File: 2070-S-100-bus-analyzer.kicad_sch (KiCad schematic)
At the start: 3 parts, among them J1 S100

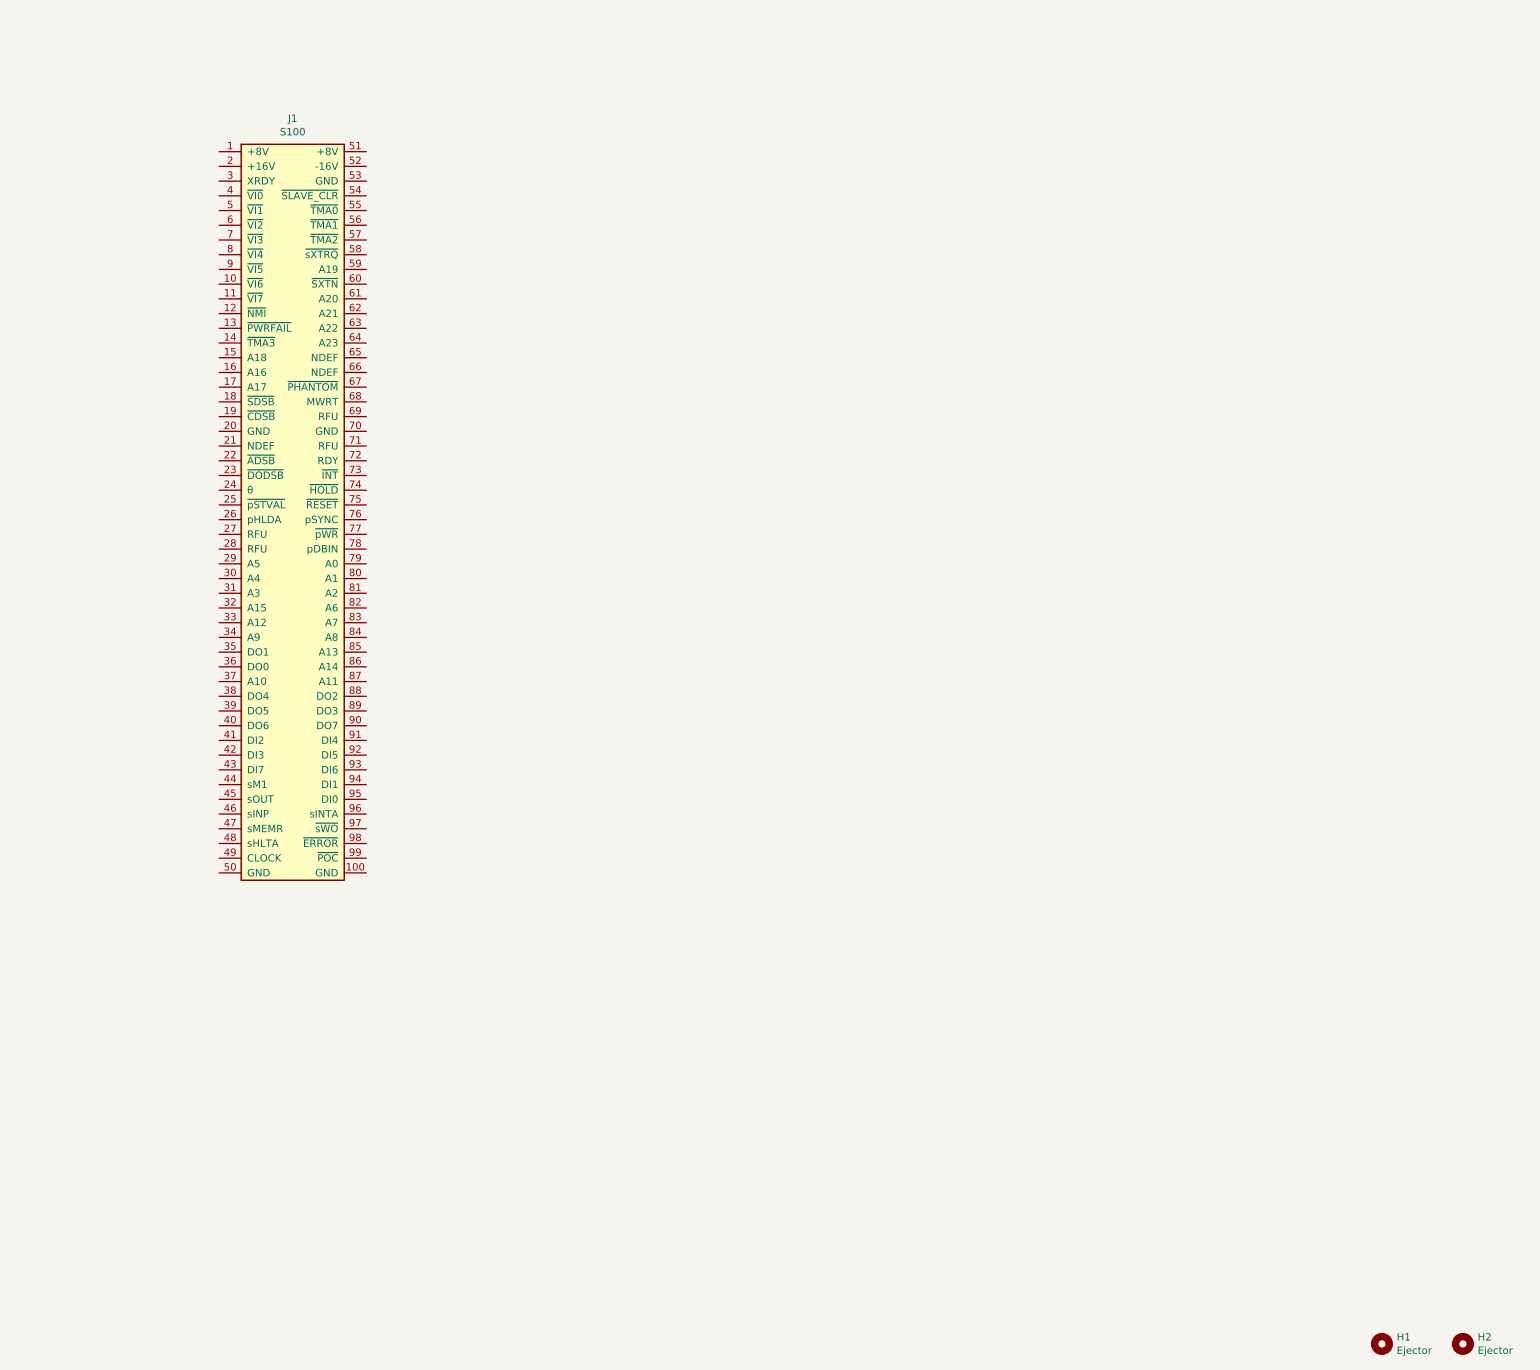
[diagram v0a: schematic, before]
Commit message: Re-start project from new KiCad9 S-100 template
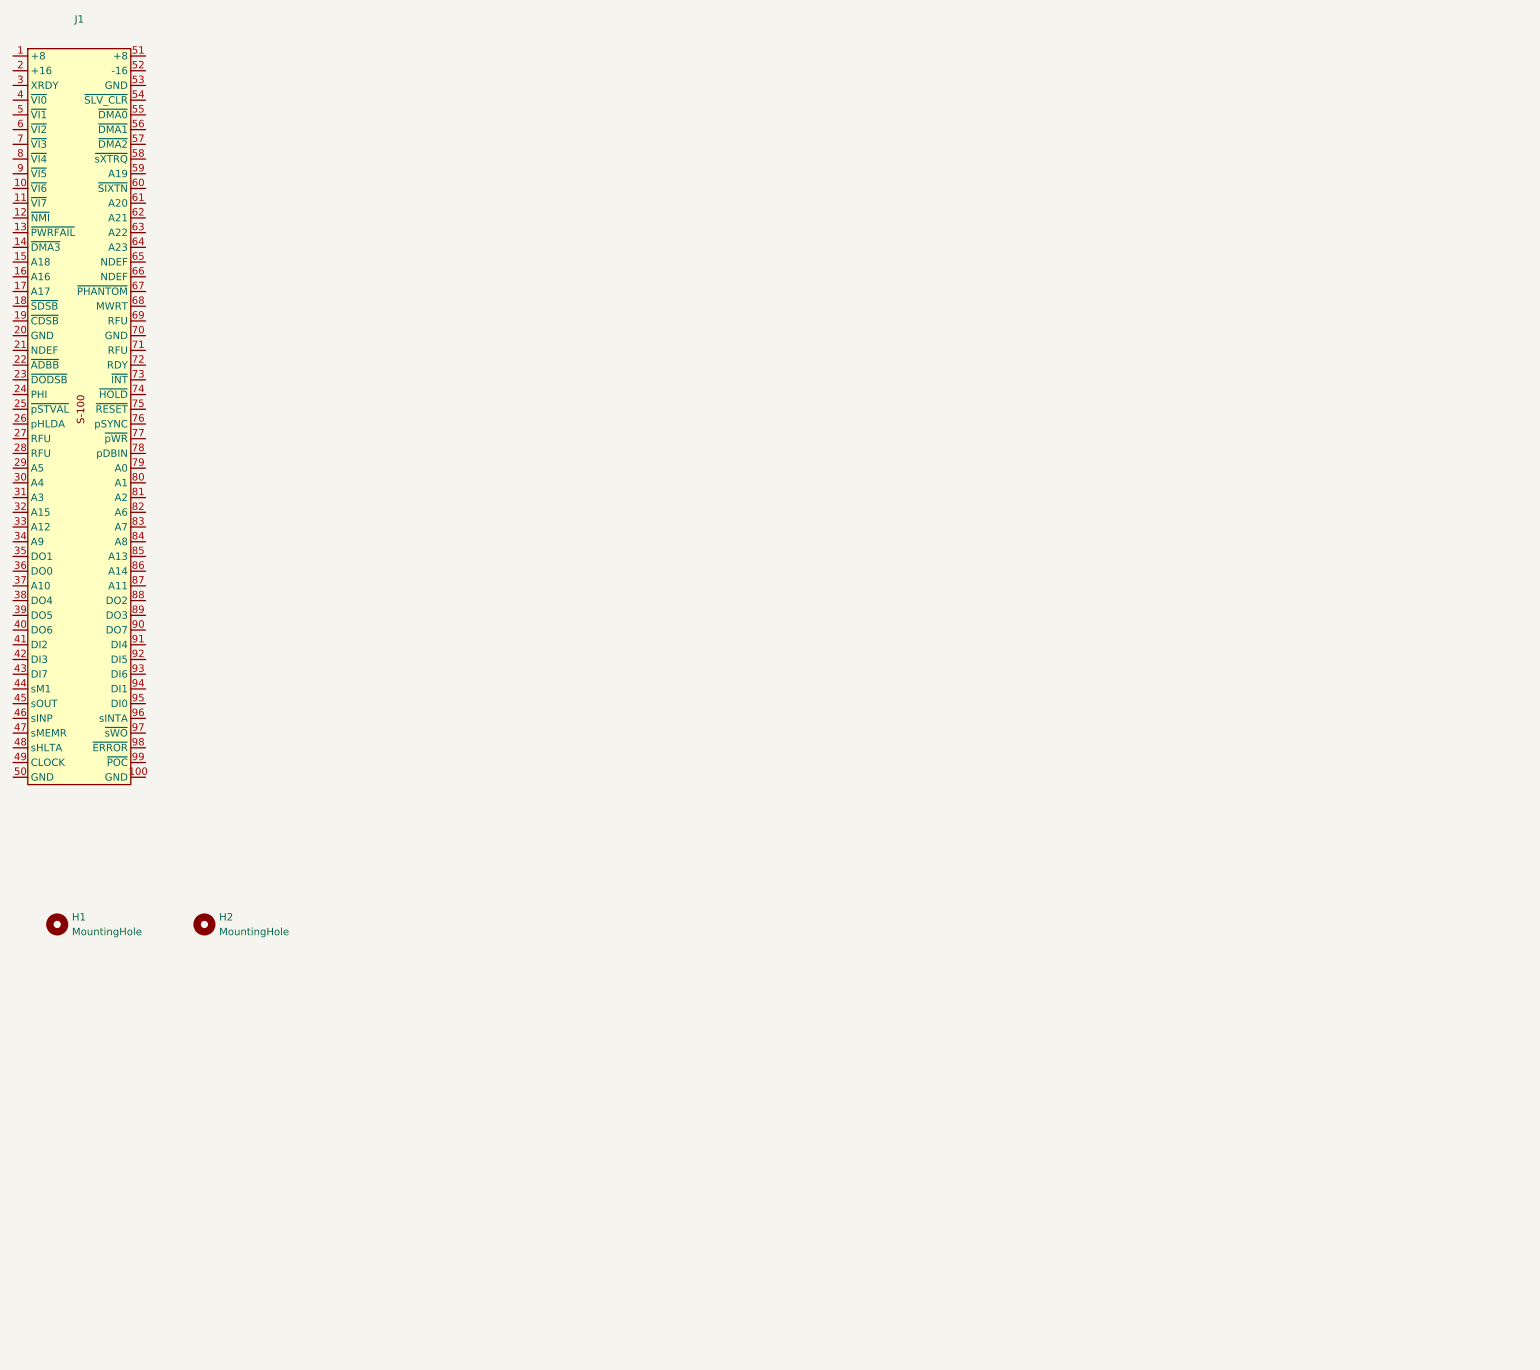
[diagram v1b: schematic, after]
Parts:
- removed J1: S100, jb-footprint:S100_MALE, symbol S-100-Template-rescue:S100-jb-symbol-S-100-Template-rescue
- added J1: ~, S100-footprints:S100-Edge-Connector, symbol S100:S100-Edge-Connector
- H1, H2: value Ejector -> MountingHole; footprint jb-footprint:MountingHole_2.7mm_M2.5 -> MountingHole:MountingHole_2.5mm; now left out of the parts list

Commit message: Checkpoint
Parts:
- added A1, A2, A3, A4, A5: RaspberryPi_Pico, Module:RaspberryPi_Pico_Common_Unspecified, symbol MCU_Module:RaspberryPi_Pico
- added D1, D2, D3: LED_Filled, LED_SMD:LED_0805_2012Metric_Pad1.15x1.40mm_HandSolder, symbol Device:LED_Filled
- added J10, J11, J2, J3, J4, J5, J6, J7, J8, J9: Conn_02x13_Odd_Even, Connector_PinHeader_2.54mm:PinHeader_2x13_P2.54mm_Vertical, symbol Connector_Generic:Conn_02x13_Odd_Even
- added U1, U10, U11, U12, U13, U14, U15, U2, U3, U4, U5, U6, U7, U8, U9: 74LVCH245APW,118, Package_SO:TSSOP-20_4.4x6.5mm_P0.65mm, symbol Logic_LevelTranslator:SN74LVC245APW
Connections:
- net at J1.10 (~{VI6}): now also J2.15 (Pin_15)
- net GND: now reaches J1.100 (GND)
- net GND: now also J1.50 (GND), J2.25 (Pin_25), J2.26 (Pin_26), J3.25 (Pin_25), J3.26 (Pin_26), J4.25 (Pin_25), J4.26 (Pin_26), J5.25 (Pin_25), J5.26 (Pin_26), J6.25 (Pin_25), J6.26 (Pin_26), J7.25 (Pin_25), J7.26 (Pin_26), J8.25 (Pin_25), J8.26 (Pin_26), J9.25 (Pin_25), J9.26 (Pin_26), U1.1 (DIR), U1.19 (~{OE})
- net at J1.11 (~{VI7}): now also J2.17 (Pin_17)
- net at J1.12 (~{NMI}): now also J2.19 (Pin_19)
- net at J1.13 (~{PWRFAIL}): now also J2.21 (Pin_21)
- net at J1.14 (~{DMA3}): now also J2.23 (Pin_23)
- net at J1.15 (A18): now also J3.1 (Pin_1)
- net at J1.16 (A16): now also J3.3 (Pin_3)
- net at J1.17 (A17): now also J3.5 (Pin_5)
- net at J1.18 (~{SDSB}): now also J3.7 (Pin_7)
- net at J1.19 (~{CDSB}): now also J3.9 (Pin_9)
- net at J1.20 (GND): now also J3.11 (Pin_11)
- net at J1.21 (NDEF): now also J3.13 (Pin_13)
- net at J1.22 (~{ADSB}): now also J3.15 (Pin_15)
- net at J1.23 (~{DODSB}): now also J3.17 (Pin_17)
- net at J1.24 (PHI): now also J3.19 (Pin_19)
- net at J1.25 (~{pSTVAL}): now also J3.21 (Pin_21)
- net at J1.26 (pHLDA): now also J3.23 (Pin_23)
- net at J1.27 (RFU): now also J4.1 (Pin_1)
- net at J1.28 (RFU): now also J4.3 (Pin_3)
- net at J1.29 (A5): now also J4.5 (Pin_5)
- net at J1.3 (XRDY): now also J2.1 (Pin_1)
- net at J1.30 (A4): now also J4.7 (Pin_7)
- net at J1.31 (A3): now also J4.9 (Pin_9)
- net at J1.32 (A15): now also J4.11 (Pin_11)
- net at J1.33 (A12): now also J4.13 (Pin_13)
- net at J1.34 (A9): now also J4.15 (Pin_15)
- net at J1.35 (DO1): now also J4.17 (Pin_17)
- net at J1.36 (DO0): now also J4.19 (Pin_19)
- net at J1.37 (A10): now also J4.21 (Pin_21)
- net at J1.38 (DO4): now also J4.23 (Pin_23)
- net at J1.39 (DO5): now also J5.1 (Pin_1)
- net at J1.4 (~{VI0}): now also J2.3 (Pin_3)
- net at J1.40 (DO6): now also J5.3 (Pin_3)
- net at J1.41 (DI2): now also J5.5 (Pin_5)
- net at J1.42 (DI3): now also J5.7 (Pin_7)
- net at J1.43 (DI7): now also J5.9 (Pin_9)
- net at J1.44 (sM1): now also J5.11 (Pin_11)
- net at J1.45 (sOUT): now also J5.13 (Pin_13)
- net at J1.46 (sINP): now also J5.15 (Pin_15)
- net at J1.47 (sMEMR): now also J5.17 (Pin_17)
- net at J1.48 (sHLTA): now also J5.19 (Pin_19)
- net at J1.49 (CLOCK): now also J5.21 (Pin_21)
- net at J1.5 (~{VI1}): now also J2.5 (Pin_5)
- net at J1.53 (GND): now also J6.1 (Pin_1)
- net at J1.54 (~{SLV_CLR}): now also J6.3 (Pin_3)
- net at J1.55 (~{DMA0}): now also J6.5 (Pin_5)
- net at J1.56 (~{DMA1}): now also J6.7 (Pin_7)
- net at J1.57 (~{DMA2}): now also J6.9 (Pin_9)
- net at J1.58 (~{sXTRQ}): now also J6.11 (Pin_11)
- net at J1.59 (A19): now also J6.13 (Pin_13)
- net at J1.6 (~{VI2}): now also J2.7 (Pin_7)
- net at J1.60 (~{SIXTN}): now also J6.15 (Pin_15)
- net at J1.61 (A20): now also J6.17 (Pin_17)
- net at J1.62 (A21): now also J6.19 (Pin_19)
- net at J1.63 (A22): now also J6.21 (Pin_21)
- net at J1.64 (A23): now also J6.23 (Pin_23)
- net at J1.65 (NDEF): now also J7.1 (Pin_1)
- net at J1.66 (NDEF): now also J7.3 (Pin_3)
- net at J1.67 (~{PHANTOM}): now also J7.5 (Pin_5)
- net at J1.68 (MWRT): now also J7.7 (Pin_7)
- net at J1.69 (RFU): now also J7.9 (Pin_9)
- net at J1.7 (~{VI3}): now also J2.9 (Pin_9)
- net at J1.70 (GND): now also J7.11 (Pin_11)
- net at J1.71 (RFU): now also J7.13 (Pin_13)
- net at J1.72 (RDY): now also J7.15 (Pin_15)
- net at J1.73 (~{INT}): now also J7.17 (Pin_17)
- net at J1.74 (~{HOLD}): now also J7.19 (Pin_19)
- net at J1.75 (~{RESET}): now also J7.21 (Pin_21)
- net at J1.76 (pSYNC): now also J7.23 (Pin_23)
- net at J1.77 (~{pWR}): now also J8.1 (Pin_1)
- net at J1.78 (pDBIN): now also J8.3 (Pin_3)
- net at J1.79 (A0): now also J8.5 (Pin_5)
- net at J1.8 (~{VI4}): now also J2.11 (Pin_11)
- net at J1.80 (A1): now also J8.7 (Pin_7)
- net at J1.81 (A2): now also J8.9 (Pin_9)
- net at J1.82 (A6): now also J8.11 (Pin_11)
- net at J1.83 (A7): now also J8.13 (Pin_13)
- net at J1.84 (A8): now also J8.15 (Pin_15)
- net at J1.85 (A13): now also J8.17 (Pin_17)
- net at J1.86 (A14): now also J8.19 (Pin_19)
- net at J1.87 (A11): now also J8.21 (Pin_21)
- net at J1.88 (DO2): now also J8.23 (Pin_23)
- net at J1.89 (DO3): now also J9.1 (Pin_1)
- net at J1.9 (~{VI5}): now also J2.13 (Pin_13)
- net at J1.90 (DO7): now also J9.3 (Pin_3)
- net at J1.91 (DI4): now also J9.5 (Pin_5)
- net at J1.92 (DI5): now also J9.7 (Pin_7)
- net at J1.93 (DI6): now also J9.9 (Pin_9)
- net at J1.94 (DI1): now also J9.11 (Pin_11)
- net at J1.95 (DI0): now also J9.13 (Pin_13)
- net at J1.96 (sINTA): now also J9.15 (Pin_15)
- net at J1.97 (~{sWO}): now also J9.17 (Pin_17)
- net at J1.98 (~{ERROR}): now also J9.19 (Pin_19)
- net at J1.99 (~{POC}): now also J9.21 (Pin_21)
- new net: A3.13 (GND), A3.18 (GND), A3.23 (GND), A3.28 (GND), A3.3 (GND), A3.38 (GND), A3.8 (GND)
- new net: A4.13 (GND), A4.18 (GND), A4.23 (GND), A4.28 (GND), A4.3 (GND), A4.38 (GND), A4.8 (GND)
- new net: A5.36 (3V3), U13.20 (VCC), U14.20 (VCC), U15.20 (VCC)
- new net: A1.1 (GPIO0), A1.2 (GPIO1)
- new net: A1.10 (GPIO7), U1.13 (B6)
- new net: A1.11 (GPIO8), U1.12 (B7)
- new net: A1.12 (GPIO9), U1.11 (B8)
- new net: A1.13 (GND), A1.18 (GND), A1.23 (GND), A1.28 (GND), A1.3 (GND), A1.38 (GND), A1.8 (GND)
- new net: A1.14 (GPIO10), U2.18 (B1)
- new net: A1.15 (GPIO11), U2.17 (B2)
- new net: A1.16 (GPIO12), U2.16 (B3)
- new net: A1.17 (GPIO13), U2.15 (B4)
- new net: A1.19 (GPIO14), U2.14 (B5)
- new net: A1.20 (GPIO15), U2.13 (B6)
- new net: A1.21 (GPIO16), U2.12 (B7)
- new net: A1.22 (GPIO17), U2.11 (B8)
- new net: A1.24 (GPIO18), U3.18 (B1)
- new net: A1.25 (GPIO19), U3.17 (B2)
- new net: A1.26 (GPIO20), U3.16 (B3)
- new net: A1.27 (GPIO21), U3.15 (B4)
- new net: A1.29 (GPIO22), U3.14 (B5)
- new net: A1.31 (GPIO26_ADC0), U3.13 (B6)
- new net: A1.32 (GPIO27_ADC1), U3.12 (B7)
- new net: A1.34 (GPIO28_ADC2), U3.11 (B8)
- new net: A1.4 (GPIO2), U1.18 (B1)
- new net: A1.5 (GPIO3), U1.17 (B2)
- new net: A1.6 (GPIO4), U1.16 (B3)
- new net: A1.7 (GPIO5), U1.15 (B4)
- new net: A1.9 (GPIO6), U1.14 (B5)
- new net: A2.13 (GND), A2.18 (GND), A2.23 (GND), A2.28 (GND), A2.3 (GND), A2.38 (GND), A2.8 (GND)
- new net: A5.13 (GND), A5.18 (GND), A5.23 (GND), A5.28 (GND), A5.3 (GND), A5.38 (GND), A5.8 (GND)
- new net A0: J8.6 (Pin_6)
- new net A1: J8.8 (Pin_8)
- new net A10: J4.22 (Pin_22)
- new net A11: J8.22 (Pin_22)
- new net A12: J4.14 (Pin_14)
- new net A13: J8.18 (Pin_18)
- new net A14: J8.20 (Pin_20)
- new net A15: J4.12 (Pin_12)
- new net A16: J3.4 (Pin_4)
- new net A17: J3.6 (Pin_6)
- new net A18: J3.2 (Pin_2)
- new net A19: J6.14 (Pin_14), U2.7 (A6)
- new net A2: J8.10 (Pin_10)
- new net A20: J6.18 (Pin_18), U3.3 (A2)
- new net A21: J6.20 (Pin_20), U3.5 (A4)
- new net A22: J6.22 (Pin_22), U3.7 (A6)
- new net A23: J6.24 (Pin_24), U3.9 (A8)
- new net A3: J4.10 (Pin_10)
- new net A4: J4.8 (Pin_8)
- new net A5: J4.6 (Pin_6)
- new net A6: J8.12 (Pin_12)
- new net A7: J8.14 (Pin_14)
- new net A8: J8.16 (Pin_16)
- new net A9: J4.16 (Pin_16)
- new net CLOCK: J5.22 (Pin_22)
- new net DI0: J9.14 (Pin_14)
- new net DI1: J9.12 (Pin_12)
- new net DI2: J5.6 (Pin_6)
- new net DI3: J5.8 (Pin_8)
- new net DI4: J9.6 (Pin_6)
- new net DI5: J9.8 (Pin_8)
- new net DI6: J9.10 (Pin_10)
- new net DI7: J5.10 (Pin_10)
- new net DO0: J4.20 (Pin_20)
- new net DO1: J4.18 (Pin_18)
- new net DO2: J8.24 (Pin_24)
- new net DO3: J9.2 (Pin_2)
- new net DO4: J4.24 (Pin_24)
- new net DO5: J5.2 (Pin_2)
- new net DO6: J5.4 (Pin_4)
- new net DO7: J9.4 (Pin_4)
- new net MWRT: J7.8 (Pin_8)
- new net PHI: J3.20 (Pin_20)
- new net RDY: J7.16 (Pin_16)
- new net S20: J3.12 (Pin_12)
- new net S21: J3.14 (Pin_14)
- new net S27: J4.2 (Pin_2)
- new net S28: J4.4 (Pin_4)
- new net S53: J6.2 (Pin_2), U1.3 (A2)
- new net S65: J7.2 (Pin_2)
- new net S66: J7.4 (Pin_4)
- new net S69: J7.10 (Pin_10)
- new net S70: J7.12 (Pin_12)
- new net S71: J7.14 (Pin_14)
- new net VSYS: A1.39 (VSYS), A2.39 (VSYS), A3.39 (VSYS), A4.39 (VSYS), A5.39 (VSYS)
- new net XRDY: J2.2 (Pin_2), U1.2 (A1)
- new net sHLTA: J5.20 (Pin_20)
- new net sINP: J5.16 (Pin_16)
- new net sINTA: J9.16 (Pin_16)
- new net sM1: J5.12 (Pin_12)
- new net sMEMR: J5.18 (Pin_18)
- new net sOUT: J5.14 (Pin_14)
- new net ~{ADSB}: J3.16 (Pin_16)
- new net ~{CDSB}: J3.10 (Pin_10)
- new net ~{DMA0}: J6.6 (Pin_6), U1.7 (A6)
- new net ~{DMA1}: J6.8 (Pin_8), U1.9 (A8)
- new net ~{DMA2}: J6.10 (Pin_10), U2.3 (A2)
- new net ~{DMA3}: J2.24 (Pin_24), U3.8 (A7)
- new net ~{DODSB}: J3.18 (Pin_18)
- new net ~{ERROR}: J9.20 (Pin_20)
- new net ~{HOLD}: J7.20 (Pin_20)
- new net ~{INT}: J2.20 (Pin_20), J7.18 (Pin_18), U3.4 (A3)
- new net ~{PHANTOM}: J7.6 (Pin_6)
- new net ~{PICO_RESET}: A5.30 (RUN)
- new net ~{POC}: J9.22 (Pin_22)
- new net ~{PWRFAIL}: J2.22 (Pin_22), U3.6 (A5)
- new net ~{RESET}: J7.22 (Pin_22)
- new net ~{SDSB}: J3.8 (Pin_8)
- new net ~{SIXTN}: J6.16 (Pin_16), U2.9 (A8)
- new net ~{SLV_CLR}: J6.4 (Pin_4), U1.5 (A4)
- new net ~{VI0}: J2.4 (Pin_4), U1.4 (A3)
- new net ~{VI1}: J2.6 (Pin_6), U1.6 (A5)
- new net ~{VI2}: J2.8 (Pin_8), U1.8 (A7)
- new net ~{VI3}: J2.10 (Pin_10), U2.2 (A1)
- new net ~{VI4}: J2.12 (Pin_12), U2.4 (A3)
- new net ~{VI5}: J2.14 (Pin_14), U2.6 (A5)
- new net ~{VI6}: J2.16 (Pin_16), U2.8 (A7)
- new net ~{VI7}: J2.18 (Pin_18), U3.2 (A1)
- new net ~{pDBIN}: J8.4 (Pin_4)
- new net ~{pHLDA}: J3.24 (Pin_24)
- new net ~{pSTVAL}: J3.22 (Pin_22)
- new net ~{pSYNC}: J7.24 (Pin_24)
- new net ~{pWR}: J8.2 (Pin_2)
- new net ~{sWO}: J9.18 (Pin_18)
- new net ~{sXTRQ}: J6.12 (Pin_12), U2.5 (A4)
- no-connect marks 0 -> 5
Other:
- moved on the sheet: H1, H2, J1

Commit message: Add S100 power
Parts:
- added C31: .1uF, Capacitor_SMD:C_0603_1608Metric_Pad1.08x0.95mm_HandSolder, symbol Device:C
- added C33: 47pF, Capacitor_SMD:C_0603_1608Metric_Pad1.08x0.95mm_HandSolder, symbol Device:C
- added C47: 10uF, Capacitor_SMD:C_0805_2012Metric_Pad1.18x1.45mm_HandSolder, symbol Device:C
- added C50, C58, C66, C67: 22uF, Capacitor_SMD:C_0805_2012Metric_Pad1.18x1.45mm_HandSolder, symbol Device:C
- added D4: SS56F, Diode_SMD:D_SMB_Handsoldering, symbol Device:D_Schottky_Filled
- added L11: 6.8uH, Inductor_SMD:L_Bourns-SRN6028, symbol Device:L
- added R1, R2, R3: 1K, Resistor_SMD:R_0603_1608Metric_Pad0.98x0.95mm_HandSolder, symbol Device:R
- added R47: 8K4, Resistor_SMD:R_0603_1608Metric_Pad0.98x0.95mm_HandSolder, symbol Device:R
- added R48: 1K6, Resistor_SMD:R_0603_1608Metric_Pad0.98x0.95mm_HandSolder, symbol Device:R
- added U16: AP63300, Package_TO_SOT_SMD:SOT-23-6, symbol jb-symbol:AP63300
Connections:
- net GND: now also D1.1 (K), D2.1 (K), D3.1 (K), C47.2, C50.2, C58.2, C66.2, C67.2, R48.2, U16.4 (GND)
- net at D3.2 (A): now also R2.2
- net +S100_8V: now reaches J1.1 (+8)
- net +S100_8V: now also J1.51 (+8), C47.1, C66.1, C67.1, U16.3 (VIN)
- net at A4.36 (3V3): now also U10.20 (VCC), U11.20 (VCC), U12.20 (VCC)
- net at D1.2 (A): now also R3.2
- net at A1.36 (3V3): now also U1.20 (VCC), U2.20 (VCC), U3.20 (VCC)
- net at D2.2 (A): now also R1.2
- net VSYS renamed +VSYS
- net +VSYS: now also D4.1 (K)
- new net: C33.2, R47.2, R48.1, U16.1 (FB)
- new net: C31.1, U16.6 (BST)
- new net: C31.2, L11.1, U16.5 (SW)
- new net +S100_5V: C33.1, C50.1, C58.1, D4.2 (A), L11.2, R3.1, R47.1
- no-connect marks 5 -> 7
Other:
- note added: "5V @ 3A"
- moved on the sheet: D1, D2

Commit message: Checkpoint
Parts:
- added C1, C10, C11, C12, C13, C14, C15, C2, C3, C4, C5, C6, C7, C8, C9: .1uF, Capacitor_SMD:C_0603_1608Metric_Pad1.08x0.95mm_HandSolder, symbol Device:C
- added D5: SS56F, Diode_SMD:D_SMB_Handsoldering, symbol Device:D_Schottky_Filled
- added J12: USB4105-GF-A, Connector_USB:USB_C_Receptacle_GCT_USB4105-xx-A_16P_TopMnt_Horizontal, symbol Connector:USB_C_Receptacle_PowerOnly_24P
- added J13, J14: Conn_01x01, Connector_PinHeader_2.54mm:PinHeader_1x01_P2.54mm_Vertical, symbol Connector_Generic:Conn_01x01
- added J15, J16, J17, J18, J19: Conn_01x02, Connector_PinHeader_2.54mm:PinHeader_1x02_P2.54mm_Vertical, symbol Connector_Generic:Conn_01x02
- added R10, R6, R7, R8, R9: 1K, Resistor_SMD:R_0603_1608Metric_Pad0.98x0.95mm_HandSolder, symbol Device:R
- added R4, R5: 5K1, Resistor_SMD:R_0603_1608Metric_Pad0.98x0.95mm_HandSolder, symbol Device:R
- added SW1: SW_MEC_5E, S100-footprints:tactile, symbol Switch:SW_MEC_5E
- added U17: LM7805_TO220, Package_TO_SOT_THT:TO-220-3_Horizontal_TabDown, symbol Regulator_Linear:LM7805_TO220
- D4: Digi-Key_PN (none) -> 5399-SS56FCT-ND
- H1, H2: value MountingHole -> Card Ejector; Digi-Key_PN (none) -> 492-1025-ND; now in the parts list
- U1, U10, U11, U12, U13, U14, U15, U2, U3, U4, U5, U6, U7, U8, U9: Digi-Key_PN (none) -> 1727-4041-1-ND
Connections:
- net +S100_5V: now also R1.1, U17.3 (VO); no longer R3.1
- net +S100_8V: now also U17.1 (VI)
- net +VSYS: now also R2.1, D5.1 (K)
- net A0: now also U7.7 (A6)
- net A1: now also U7.9 (A8)
- net A10: now also U9.6 (A5)
- net A11: now also U9.7 (A6)
- net A12: now also U8.6 (A5)
- net A13: now also U9.3 (A2)
- net A14: now also U9.5 (A4)
- net A15: now also U8.4 (A3)
- net A16: now also U4.4 (A3)
- net A17: now also U4.6 (A5)
- net A18: now also U4.2 (A1)
- net A2: now also U8.3 (A2)
- net A3: now also U8.2 (A1)
- net A4: now also U7.8 (A7)
- net A5: now also U7.6 (A5)
- net A6: now also U8.5 (A4)
- net A7: now also U8.7 (A6)
- net A8: now also U8.9 (A8)
- net A9: now also U8.8 (A7)
- net CLOCK: now also U12.6 (A5)
- net DI0: now also U11.7 (A6)
- net DI1: now also U11.5 (A4)
- net DI2: now also U10.6 (A5)
- net DI3: now also U10.8 (A7)
- net DI4: now also U10.7 (A6)
- net DI5: now also U10.9 (A8)
- net DI6: now also U11.3 (A2)
- net DI7: now also U11.2 (A1)
- net DO0: now also U9.4 (A3)
- net DO1: now also U9.2 (A1)
- net DO2: now also U9.9 (A8)
- net DO3: now also U10.3 (A2)
- net DO4: now also U9.8 (A7)
- net DO5: now also U10.2 (A1)
- net DO6: now also U10.4 (A3)
- net DO7: now also U10.5 (A4)
- net GND: now also A1.13 (GND), A1.18 (GND), A1.23 (GND), A1.28 (GND), A1.3 (GND), A1.33 (AGND), A1.38 (GND), A1.8 (GND), A2.13 (GND), A2.18 (GND), A2.23 (GND), A2.28 (GND), A2.3 (GND), A2.33 (AGND), A2.38 (GND), A2.8 (GND), A3.13 (GND), A3.18 (GND), A3.23 (GND), A3.28 (GND), A3.3 (GND), A3.33 (AGND), A3.38 (GND), A3.8 (GND), A4.13 (GND), A4.18 (GND), A4.23 (GND), A4.28 (GND), A4.3 (GND), A4.33 (AGND), A4.38 (GND), A4.8 (GND), A5.13 (GND), A5.18 (GND), A5.23 (GND), A5.28 (GND), A5.3 (GND), A5.33 (AGND), A5.38 (GND), A5.8 (GND), J10.25 (Pin_25), J10.26 (Pin_26), J11.25 (Pin_25), J11.26 (Pin_26), U1.10 (GND), U10.10 (GND), U10.19 (~{OE}), U11.10 (GND), U11.19 (~{OE}), U12.10 (GND), U12.19 (~{OE}), U13.10 (GND), U13.19 (~{OE}), U14.10 (GND), U14.19 (~{OE}), U15.10 (GND), U15.19 (~{OE}), U2.10 (GND), U2.19 (~{OE}), U3.10 (GND), U3.19 (~{OE}), U4.10 (GND), U4.19 (~{OE}), U5.10 (GND), U5.19 (~{OE}), U6.10 (GND), U6.19 (~{OE}), U7.10 (GND), U7.19 (~{OE}), U8.10 (GND), U8.19 (~{OE}), U9.10 (GND), U9.19 (~{OE}), C1.2, C10.2, C11.2, C12.2, C13.2, C14.2, C15.2, C2.2, C3.2, C4.2, C5.2, C6.2, C7.2, C8.2, C9.2, J12.A1 (GND), J12.A12 (GND), J12.B1 (GND), J12.B12 (GND), J12.S1 (SHIELD), J13.1 (Pin_1), J14.1 (Pin_1), R4.2, R5.2, SW1.3 (K), SW1.4 (A), U17.2 (GND); no longer U1.1 (DIR)
- net MWRT: now also U4.9 (A8)
- net PHI: now also U6.4 (A3)
- net RDY: now also U5.9 (A8)
- net S20: now also U5.4 (A3)
- net S21: now also U5.6 (A5)
- net S27: now also U7.2 (A1)
- net S28: now also U7.4 (A3)
- net S65: now also U4.3 (A2)
- net S66: now also U4.5 (A4)
- net S69: now also U5.3 (A2)
- net S70: now also U5.5 (A4)
- net S71: now also U5.7 (A6)
- net sHLTA: now also U12.4 (A3)
- net sINP: now also U11.8 (A7)
- net sINTA: now also U11.9 (A8)
- net sM1: now also U11.4 (A3)
- net sMEMR: now also U12.2 (A1)
- net sOUT: now also U11.6 (A5)
- net ~{ADSB}: now also U5.8 (A7)
- net ~{CDSB}: now also U5.2 (A1)
- net ~{DODSB}: now also U6.2 (A1)
- net ~{ERROR}: now also U12.5 (A4)
- net ~{HOLD}: now also U6.5 (A4)
- net ~{INT}: now also U6.3 (A2); no longer J2.20 (Pin_20), U3.4 (A3)
- net ~{PHANTOM}: now also U4.7 (A6)
- net ~{PICO_RESET}: now also A1.30 (RUN), A2.30 (RUN), A3.30 (RUN), A4.30 (RUN), SW1.2
- net ~{POC}: now also U12.7 (A6)
- net ~{RESET}: now also U6.7 (A6)
- net ~{SDSB}: now also U4.8 (A7)
- net ~{pDBIN}: now also U7.5 (A4)
- net ~{pHLDA}: now also U6.8 (A7)
- net ~{pSTVAL}: now also U6.6 (A5)
- net ~{pSYNC}: now also U6.9 (A8)
- net ~{pWR}: now also U7.3 (A2)
- net ~{sWO}: now also U12.3 (A2)
- net at R3.2: now also D3.2 (A); no longer D1.2 (A)
- net at A3.1 (GPIO0): now also A3.2 (GPIO1), J17.1 (Pin_1)
- net at A3.10 (GPIO7): now also U7.13 (B6)
- net at A3.11 (GPIO8): now also U7.12 (B7)
- net at A3.12 (GPIO9): now also U7.11 (B8)
- net at A3.14 (GPIO10): now also U8.18 (B1)
- net at A3.15 (GPIO11): now also U8.17 (B2)
- net at A3.16 (GPIO12): now also U8.16 (B3)
- net at A3.17 (GPIO13): now also U8.15 (B4)
- net at A3.19 (GPIO14): now also U8.14 (B5)
- net at A3.20 (GPIO15): now also U8.13 (B6)
- net at A3.21 (GPIO16): now also U8.12 (B7)
- net at A3.22 (GPIO17): now also U8.11 (B8)
- net at A3.24 (GPIO18): now also U9.18 (B1)
- net at A3.25 (GPIO19): now also U9.17 (B2)
- net at A3.26 (GPIO20): now also U9.16 (B3)
- net at A3.27 (GPIO21): now also U9.15 (B4)
- net at A3.29 (GPIO22): now also U9.14 (B5)
- net at A3.31 (GPIO26_ADC0): now also U9.13 (B6)
- net at A3.32 (GPIO27_ADC1): now also U9.12 (B7)
- net at A3.34 (GPIO28_ADC2): now also U9.11 (B8)
- net at A3.36 (3V3): now also U7.20 (VCC), U8.20 (VCC), U9.20 (VCC), C7.1, C8.1, C9.1, R8.1
- net at A3.4 (GPIO2): now also U7.18 (B1)
- net at A3.5 (GPIO3): now also U7.17 (B2)
- net at A3.6 (GPIO4): now also U7.16 (B3)
- net at A3.7 (GPIO5): now also U7.15 (B4)
- net at A3.9 (GPIO6): now also U7.14 (B5)
- net at R2.2: now also D2.2 (A); no longer D3.2 (A)
- net at R1.2: now also D1.2 (A); no longer D2.2 (A)
- net at U4.1 (DIR): now also U5.1 (DIR), U6.1 (DIR), R7.2
- net at U4.11 (B8): now also A2.12 (GPIO9)
- net at U4.12 (B7): now also A2.11 (GPIO8)
- net at U4.13 (B6): now also A2.10 (GPIO7)
- net at U4.14 (B5): now also A2.9 (GPIO6)
- net at U4.15 (B4): now also A2.7 (GPIO5)
- net at U4.16 (B3): now also A2.6 (GPIO4)
- net at U4.17 (B2): now also A2.5 (GPIO3)
- net at U4.18 (B1): now also A2.4 (GPIO2)
- net at U4.20 (VCC): now also A2.36 (3V3), U5.20 (VCC), U6.20 (VCC), C4.1, C5.1, C6.1, R7.1
- net at A4.1 (GPIO0): now also A4.2 (GPIO1), J16.1 (Pin_1)
- net at A4.10 (GPIO7): now also U10.13 (B6)
- net at A4.11 (GPIO8): now also U10.12 (B7)
- net at A4.12 (GPIO9): now also U10.11 (B8)
- net at A4.14 (GPIO10): now also U11.18 (B1)
- net at A4.15 (GPIO11): now also U11.17 (B2)
- net at A4.16 (GPIO12): now also U11.16 (B3)
- net at A4.17 (GPIO13): now also U11.15 (B4)
- net at A4.19 (GPIO14): now also U11.14 (B5)
- net at A4.20 (GPIO15): now also U11.13 (B6)
- net at A4.21 (GPIO16): now also U11.12 (B7)
- net at A4.22 (GPIO17): now also U11.11 (B8)
- net at A4.24 (GPIO18): now also U12.18 (B1)
- net at A4.25 (GPIO19): now also U12.17 (B2)
- net at A4.26 (GPIO20): now also U12.16 (B3)
- net at A4.27 (GPIO21): now also U12.15 (B4)
- net at A4.29 (GPIO22): now also U12.14 (B5)
- net at A4.31 (GPIO26_ADC0): now also U12.13 (B6)
- net at A4.32 (GPIO27_ADC1): now also U12.12 (B7)
- net at A4.34 (GPIO28_ADC2): now also U12.11 (B8)
- net at A4.36 (3V3), U10.20 (VCC), U11.20 (VCC)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: now also C10.1, C11.1, C12.1, R9.1
- net at A4.4 (GPIO2): now also U10.18 (B1)
- net at A4.5 (GPIO3): now also U10.17 (B2)
- net at A4.6 (GPIO4): now also U10.16 (B3)
- net at A4.7 (GPIO5): now also U10.15 (B4)
- net at A4.9 (GPIO6): now also U10.14 (B5)
- net at U9.1 (DIR): now also U7.1 (DIR), U8.1 (DIR), R8.2
- net at U10.1 (DIR): now also U11.1 (DIR), U12.1 (DIR), R9.2
- net A4.24: now reaches J9.24 (Pin_24)
- net A4.24: now also U12.9 (A8)
- net at U13.1 (DIR): now also U14.1 (DIR), U15.1 (DIR), R10.2
- net at U13.11 (B8): now also A5.12 (GPIO9)
- net at U13.12 (B7): now also A5.11 (GPIO8)
- net at U13.13 (B6): now also A5.10 (GPIO7)
- net at U13.14 (B5): now also A5.9 (GPIO6)
- net at U13.15 (B4): now also A5.7 (GPIO5)
- net at U13.16 (B3): now also A5.6 (GPIO4)
- net at U13.17 (B2): now also A5.5 (GPIO3)
- net at U13.18 (B1): now also A5.4 (GPIO2)
- net T1: now reaches U13.2 (A1)
- net T1: now also J10.1 (Pin_1), J10.2 (Pin_2)
- net at A5.36 (3V3), U13.20 (VCC), U14.20 (VCC)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: now also C13.1, C14.1, C15.1, R10.1
- net T2: now reaches U13.3 (A2)
- net T2: now also J11.1 (Pin_1), J11.2 (Pin_2)
- net T3: now reaches U13.4 (A3)
- net T3: now also J10.3 (Pin_3), J10.4 (Pin_4)
- net T4: now reaches U13.5 (A4)
- net T4: now also J11.3 (Pin_3), J11.4 (Pin_4)
- net T5: now reaches U13.6 (A5)
- net T5: now also J10.5 (Pin_5), J10.6 (Pin_6)
- net T6: now reaches U13.7 (A6)
- net T6: now also J11.5 (Pin_5), J11.6 (Pin_6)
- net T7: now reaches U13.8 (A7)
- net T7: now also J10.7 (Pin_7), J10.8 (Pin_8)
- net T8: now reaches U13.9 (A8)
- net T8: now also J11.7 (Pin_7), J11.8 (Pin_8)
- net at U5.11 (B8): now also A2.22 (GPIO17)
- net at U5.12 (B7): now also A2.21 (GPIO16)
- net at U5.13 (B6): now also A2.20 (GPIO15)
- net at U5.14 (B5): now also A2.19 (GPIO14)
- net at U5.15 (B4): now also A2.17 (GPIO13)
- net at U5.16 (B3): now also A2.16 (GPIO12)
- net at U5.17 (B2): now also A2.15 (GPIO11)
- net at U5.18 (B1): now also A2.14 (GPIO10)
- net at A1.1 (GPIO0), A1.2 (GPIO1): now also J19.1 (Pin_1)
- net at A1.36 (3V3), U1.20 (VCC), U2.20 (VCC)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: now also C1.1, C2.1, C3.1, R6.1
- net at U2.1 (DIR): now also U1.1 (DIR), U3.1 (DIR), R6.2
- net at U14.11 (B8): now also A5.22 (GPIO17)
- net at U14.12 (B7): now also A5.21 (GPIO16)
- net at U14.13 (B6): now also A5.20 (GPIO15)
- net at U14.14 (B5): now also A5.19 (GPIO14)
- net at U14.15 (B4): now also A5.17 (GPIO13)
- net at U14.16 (B3): now also A5.16 (GPIO12)
- net at U14.17 (B2): now also A5.15 (GPIO11)
- net at U14.18 (B1): now also A5.14 (GPIO10)
- net T9: now reaches U14.2 (A1)
- net T9: now also J10.10 (Pin_10), J10.9 (Pin_9)
- net T10: now reaches U14.3 (A2)
- net T10: now also J11.10 (Pin_10), J11.9 (Pin_9)
- net T11: now reaches U14.4 (A3)
- net T11: now also J10.11 (Pin_11), J10.12 (Pin_12)
- net T12: now reaches U14.5 (A4)
- net T12: now also J11.11 (Pin_11), J11.12 (Pin_12)
- net T13: now reaches U14.6 (A5)
- net T13: now also J10.13 (Pin_13), J10.14 (Pin_14)
- net T14: now reaches U14.7 (A6)
- net T14: now also J11.13 (Pin_13), J11.14 (Pin_14)
- net T15: now reaches U14.8 (A7)
- net T15: now also J10.15 (Pin_15), J10.16 (Pin_16)
- net T16: now reaches U14.9 (A8)
- net T16: now also J11.15 (Pin_15), J11.16 (Pin_16)
- net at U15.11 (B8): now also A5.34 (GPIO28_ADC2)
- net at U15.12 (B7): now also A5.32 (GPIO27_ADC1)
- net at U15.13 (B6): now also A5.31 (GPIO26_ADC0)
- net at U15.14 (B5): now also A5.29 (GPIO22)
- net at U15.15 (B4): now also A5.27 (GPIO21)
- net at U15.16 (B3): now also A5.26 (GPIO20)
- net at U15.17 (B2): now also A5.25 (GPIO19)
- net at U15.18 (B1): now also A5.24 (GPIO18)
- net T17: now reaches U15.2 (A1)
- net T17: now also J10.17 (Pin_17), J10.18 (Pin_18)
- net T18: now reaches U15.3 (A2)
- net T18: now also J11.17 (Pin_17), J11.18 (Pin_18)
- net T19: now reaches U15.4 (A3)
- net T19: now also J10.19 (Pin_19), J10.20 (Pin_20)
- net T20: now reaches U15.5 (A4)
- net T20: now also J11.19 (Pin_19), J11.20 (Pin_20)
- net T21: now reaches U15.6 (A5)
- net T21: now also J10.21 (Pin_21), J10.22 (Pin_22)
- net T22: now reaches U15.7 (A6)
- net T22: now also J11.21 (Pin_21), J11.22 (Pin_22)
- net T23: now reaches U15.8 (A7)
- net T23: now also J10.23 (Pin_23), J10.24 (Pin_24)
- net T24: now reaches U15.9 (A8)
- net T24: now also J11.23 (Pin_23), J11.24 (Pin_24)
- net at U6.11 (B8): now also A2.34 (GPIO28_ADC2)
- net at U6.12 (B7): now also A2.32 (GPIO27_ADC1)
- net at U6.13 (B6): now also A2.31 (GPIO26_ADC0)
- net at U6.14 (B5): now also A2.29 (GPIO22)
- net at U6.15 (B4): now also A2.27 (GPIO21)
- net at U6.16 (B3): now also A2.26 (GPIO20)
- net at U6.17 (B2): now also A2.25 (GPIO19)
- net at U6.18 (B1): now also A2.24 (GPIO18)
- net A4.23: now reaches U12.8 (A7)
- net A4.23: now also J5.24 (Pin_24)
- net at A2.1 (GPIO0): now also A2.2 (GPIO1), J18.1 (Pin_1)
- net at A5.1 (GPIO0): now also A5.2 (GPIO1), J15.1 (Pin_1)
- new net: J12.A5 (CC1), R5.1
- new net: J12.B5 (CC2), R4.1
- new net +USBC5: D5.2 (A), J12.A4 (VBUS), J12.A9 (VBUS), J12.B4 (VBUS), J12.B9 (VBUS), R3.1
- new net TRIG: J15.2 (Pin_2), J16.2 (Pin_2), J17.2 (Pin_2), J18.2 (Pin_2), J19.2 (Pin_2)
- new net ~{NMI}: J2.20 (Pin_20), U3.4 (A3)
- no-connect marks 7 -> 16
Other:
- note added: "5V"
- note removed: "5V @ 3A"
- moved on the sheet: C31, C33, C47, C50, C58, C66, C67, D1, D2, D3, D4, H1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

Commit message: power supply routing
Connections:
- no-connect marks 16 -> 21
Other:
- moved on the sheet: D5
